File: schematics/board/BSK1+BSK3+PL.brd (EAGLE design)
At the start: 82 x 100 mm, 81 parts

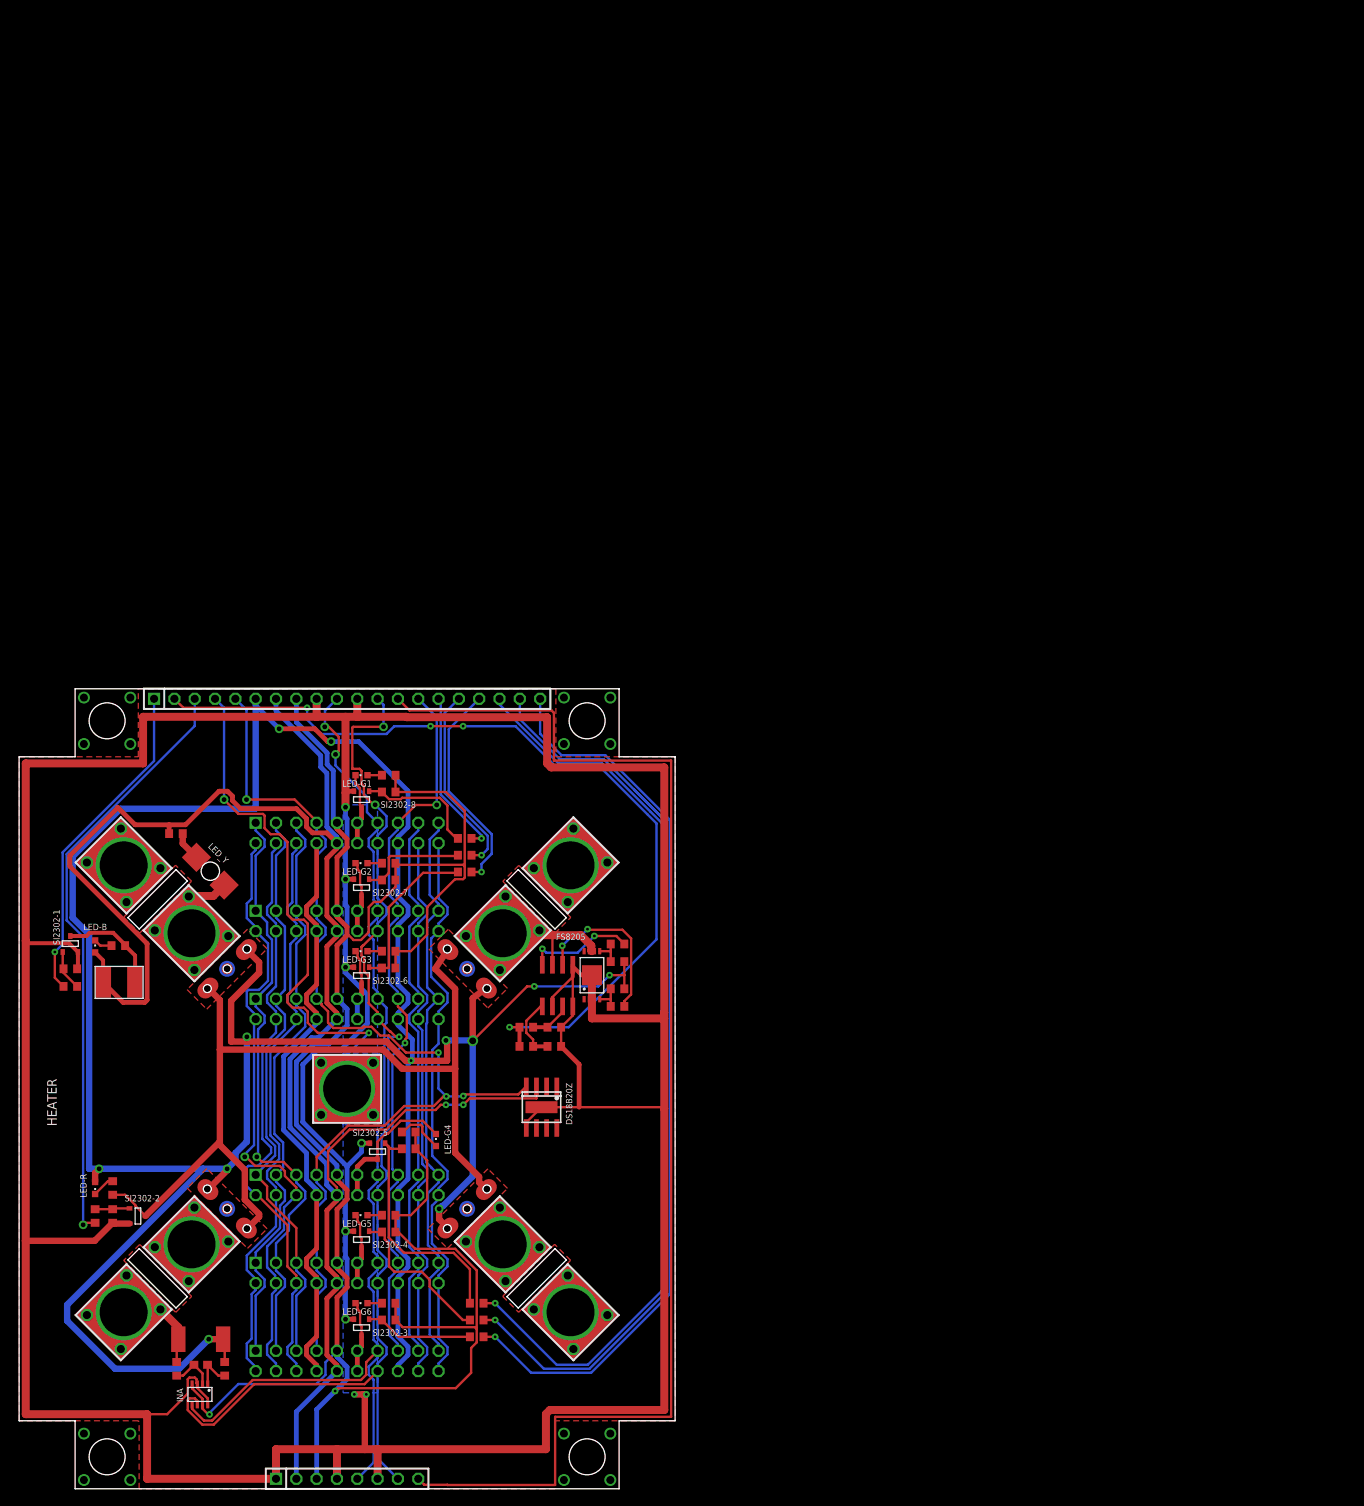
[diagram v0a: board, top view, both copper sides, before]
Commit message: Исправлены площадки механизмов Розе, соответствующие платы и герберы плат
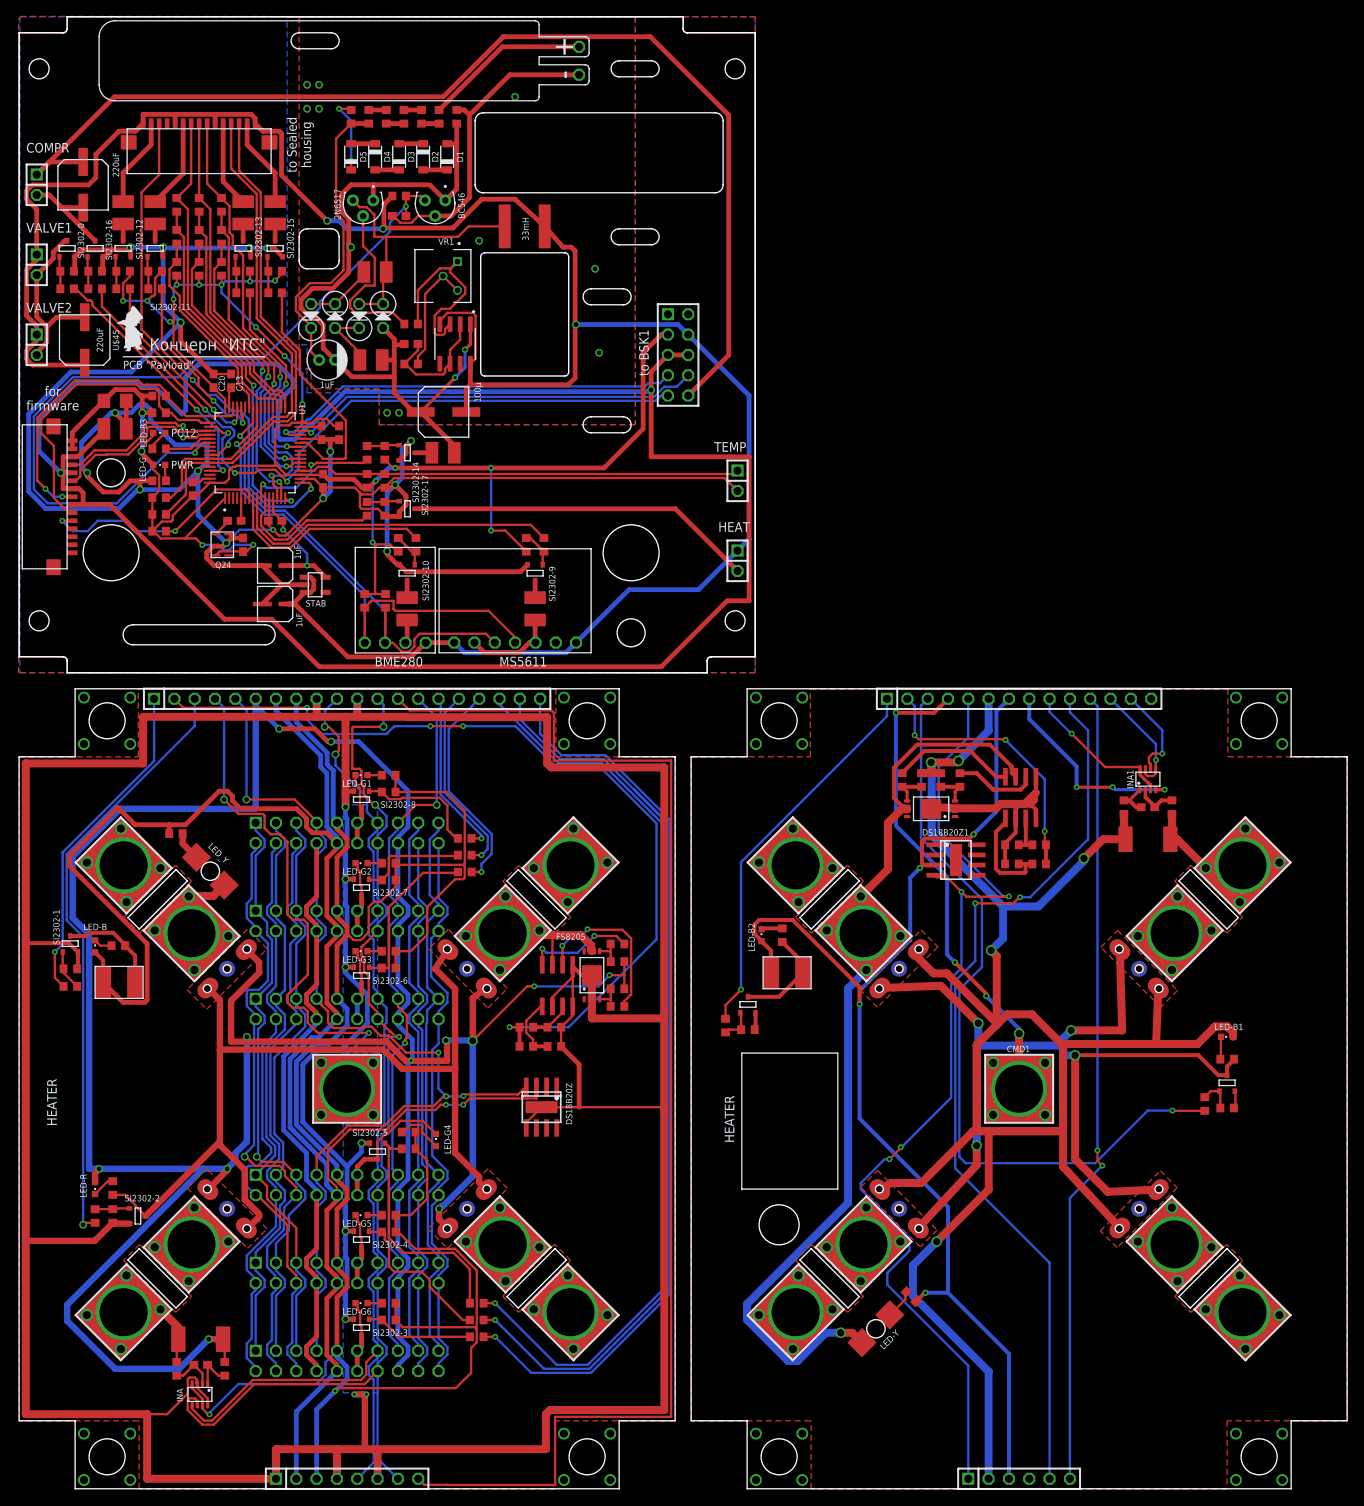
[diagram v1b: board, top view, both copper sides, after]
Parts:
- added 2N6517, BC546: DS1820, CanCubeSat:TO92/TO226
- added BKU1: (no value), pinheadCS:1X14
- added BME280: BME280BME280-PINS-ONLY, CanCubeSat:BME280-PINS-ONLY
- added BSK1: (no value), pinheadCS:1X06
- added BSK2: (no value), pinheadCS:2X05
- added C1: 0,1µ, rcl:C0603
- added C10: 10nF, rcl:C0603
- added C11: 100pF, rcl:C0603
- added C12, C14: 1uF, CanCubeSat:ECAP-SMD-D4
- added C13, C9: 2,2µ, rcl:C0603
- added C18, C2, C20, C3, C4, C6: 100nF, rcl:C0603
- added C19: 10µ, rcl:C1206
- added C5, C7: 22nF, rcl:C1210
- added C8: 1nF, rcl:C0603
- added CMD1: KCONNECTQUAD, CanCubeSat:KCONNECT_QUAD
- added COMPR, HEAT, TEMP, VALVE1, VALVE2: (no value), pinheadCS:1X02
- added D1, D2, D3, D4, D5: DIODE-MBR, CanCubeSat:SOD123
- added DS18B20Z1: DS18B20Z, CanCubeSat:SOIC8+HEAT_S
- added INA1: INA219AID, CanCubeSat:SOT23-8
- added LED-B1, LED-B2, LED-B3, LED-G: (no value), led:CHIPLED_0603
- added LED-Y: LAP4-BOTTOM, led:P47F-BOTTOM
- added MS5611: MS5611MS5611-PIN-ONLY, CanCubeSat:MS5611-PINS-ONLY
- added Q24: Q24, CanCubeSat:Q24
- added R100, R103, R105, R107, R40, R42, R58, R60, R63, R65, R68, R71, R82, R83, R84, R85, R86: 1M, resistor:R0603
- added R101, R104, R106, R108, R34, R35, R48, R49, R59, R61, R64, R66, R69, R72: 100R, resistor:R0603
- added R102, R57, R62, R67, R70, R73, R74: 0.05A, rcl:R1210
- added R109: 124k, resistor:R0603
- added R110, R81: 22k, resistor:R0603
- added R111, R112, R55, R56: 5k1, resistor:R0603
- added R36, R37, R87: 100k, resistor:R0603
- added R38, R39, R51, R54: 2k, resistor:R0603
- added R41: 1k5, resistor:R0603
- added R43: R01, rcl:R2512
- added R44, R45: 10R, resistor:R0603
- added R46, R47: 2k26, resistor:R0603
- added R50, R52, R53, R89, R90, R91, R92, R93, R96, R97, R98, R99: 10k, resistor:R0603
- added R78: 0.5A, rcl:R1210
- added R79: 1k, resistor:R0603
- added R80: 4k7, resistor:R0603
- added R88: 3k3, resistor:R0603
- added R94, R95: 200k, resistor:R0603
- added SI2302-0, SI2302-10, SI2302-11, SI2302-12, SI2302-13, SI2302-14, SI2302-15, SI2302-16, SI2302-17, SI2302-9, U$15, U$17: SI2302CDS, CanCubeSat:SOT23-3
- added STAB: ADP150AUJZ-3.3-R7, CanCubeSat:SOT23-5
- added U$10, U$11, U$12, U$5, U$6, U$7, U$8, U$9: KCONNECT, CanCubeSat:KCONNECT
- added U$13: FS8205A+, CanCubeSat:FS8205A+
- added U$14: MOCD, CanCubeSat:SOIC8
- added U$16: EM_HEAT, CanCubeSat:EM_HEAT
- added U$23, U$25, U$31, U$32: GRAFITGRAFIT4_2, CanCubeSat:GRAFIT4_2
- added U$33: PCB "BSK3", CanCubeSat:ITS-LOGO
- added U$34: 100µ, CanCubeSat:ECAP100-CMD
- added U$35, U$36, U$37, U$38: BA159, CanCubeSat:BA159
- added U$39: 1uF, CanCubeSat:ECAP1MK
- added U$40: DOSIM, CanCubeSat:DOSIM
- added U$41, U$43: FFC-CONNECT68611, CanCubeSat:68611
- added U$42: 33mH, CanCubeSat:RCH114NP
- added U$44, U$45: 220uF, CanCubeSat:ECAP220-CMD
- added U$46, U$47: PCB "Payload", CanCubeSat:ITS-LOGO
- added U1: STM32F405RGT6, STM32F405RGT6:QFP50P1200X1200X160-64N
- added U2: LMC555, LMC555CMX_NOPB:SOIC127P599X175-8N
- added VR1: 3362H-1-502LF, CanCubeSat:TRIM_3362H-1-502LF
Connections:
- new net 1: R39.2, U$15.3, U$16.2
- new net 1W1: BKU1.5, BSK1.1, DS18B20Z1.4
- new net 2: R41.2, U$17.3, U$23.P$1, U$23.P$4, U$25.P$1, U$25.P$4, U$31.P$1, U$31.P$4, U$32.P$1, U$32.P$4
- new net 3V1: BKU1.8, INA1.4
- new net 3V2: BSK2.3, C10.2, C18.2, C19.2, C2.2, C20.2, C6.2, LED-B3.A, LED-G.A, Q24.P$4, R100.2, R110.2, R111.1, R112.1, R50.2, R52.2, R53.2, R55.1, R56.1, R58.2, R60.2, R63.2, R65.2, R68.2, R71.2, R97.2, R98.2, R99.2, U$43.P$1, U$43.P$2, U1.1, U1.19, U1.32, U1.48, U1.64
- new net 4OXV: R66.1, U1.45
- new net 5V1: BKU1.7, BSK1.3, DS18B20Z1.3, LED-B2.A, R38.1, U$16.1
- new net 5V2: BME280.P$1, BSK2.4, C14.P+, HEAT.1, MS5611.P$1, MS5611.P$7, R88.1, STAB.P$1, STAB.P$3, U$34.P$2, U$41.P$1, U$41.P$10, U$41.P$15, U$41.P$5, U$42.P$1, U$45.P$1, U2.4, U2.8, VALVE1.1, VALVE2.1
- new net B3-CMD: BKU1.4, CMD1.1, CMD1.2, CMD1.3, CMD1.4, CMD1.P$1, CMD1.P$2
- new net B3-KHEAT: BKU1.1, R48.2
- new net B3-KVCC: BKU1.2, R46.2, R47.2
- new net B3-ROZE: BKU1.3, R49.2
- new net B5-KHEAT: BKU1.10, BSK1.5
- new net BME280-EXT: R61.1, U1.8
- new net BME280-INT: R101.1, U1.27
- new net BUS+1: BKU1.6, BSK1.2, LED-B1.A, R36.1, R37.2, R43.2, R44.1, U$23.P$2, U$23.P$5, U$25.P$2, U$25.P$5, U$31.P$2, U$31.P$5, U$32.P$2, U$32.P$5
- new net BUS+2: BSK2.10, COMPR.1, U$44.P$1
- new net CO: R91.1, U$41.P$7, U1.16
- new net COMPR: R106.1, U1.57
- new net CTRL-CO-1: R91.2, R96.1, U1.35
- new net CTRL-CO-2: R96.2, R97.1, U1.42
- new net CTRL-NH3-1: R90.2, R93.1, U1.33
- new net CTRL-NH3-2: R93.2, R98.1, U1.34
- new net CTRL-NO2-1: R89.2, R92.1, U1.23
- new net CTRL-NO2-2: R92.2, R99.1, U1.22
- new net DOS-G: 2N6517.1, BC546.1, C4.1, C7.2, D1.A, R73.1, R87.2, U$34.P$1, U$35.P$1, U$39.P$2, U2.1
- new net DOSE: BC546.3, C11.2, R88.2, U1.54
- new net DOSIM: R72.1, U1.10
- new net G-4OXV: R67.1, U$41.P$2
- new net G-BME: R102.1, U$41.P$14
- new net G-MICS: R74.1, U$41.P$6
- new net G-MS: R70.1, U$41.P$11
- new net GND-4OXV: R67.2, SI2302-12.3
- new net GND-BME-EXT: R62.2, SI2302-10.3
- new net GND-BME-INT: R102.2, SI2302-15.3
- new net GND-COMPR: COMPR.2, SI2302-16.3, U$44.P$2
- new net GND-DOSIM: R73.2, SI2302-14.3
- new net GND-HEAT: HEAT.2, SI2302-17.3
- new net GND-MICS: R74.2, SI2302-11.3
- new net GND-MS-EXT: R57.2, SI2302-9.3
- new net GND-MS-INT: R70.2, SI2302-13.3
- new net GND-OUT: BSK2.5, BSK2.6, R78.2, U$43.P$3, U$43.P$5, U$43.P$7, U$43.P$9
- new net GND-VALVE: SI2302-0.3, U$45.P$2, VALVE1.2, VALVE2.2
- new net GND4: BKU1.14, BKU1.9, BSK1.4, DS18B20Z1.5, DS18B20Z1.HEAT, INA1.3, INA1.8, R40.2, R42.2, R94.1, R95.1, U$13.23, U$13.HEAT, U$14.2, U$14.4, U$14.5, U$15.2, U$17.2
- new net GND9: C10.1, C12.P-, C13.1, C14.P-, C18.1, C19.1, C2.1, C20.1, C3.2, C6.1, C9.1, Q24.P$2, R103.2, R105.2, R107.2, R109.1, R54.1, R78.1, SI2302-0.2, SI2302-10.2, SI2302-11.2, SI2302-12.2, SI2302-13.2, SI2302-14.2, SI2302-15.2, SI2302-16.2, SI2302-17.2, SI2302-9.2, STAB.P$2, TEMP.2, U1.12, U1.18, U1.28, U1.60, U1.63
- new net HEAT: R108.1, U1.11
- new net MICS: R64.1, U1.44
- new net MS5611-EXT: R59.1, U1.9
- new net MS5611-INT: R69.1, U1.26
- new net N$100: R105.1, R106.2, SI2302-16.1
- new net N$101: R107.1, R108.2, SI2302-17.1
- new net N$102: C12.P+, C3.1, STAB.P$5, U1.13
- new net N$103: LED-G.C, R54.2
- new net N$33: R35.1, R36.2, U$13.5
- new net N$39: R34.1, R37.1, U$13.4
- new net N$40: LED-Y.A, R38.2
- new net N$41: LED-B2.C, R39.1
- new net N$42: LED-B1.C, R41.1
- new net N$43: C1.1, INA1.1, R44.2
- new net N$44: C1.2, INA1.2, R45.2
- new net N$45: R46.1, R94.2, U$14.1
- new net N$46: R47.1, R95.2, U$14.3
- new net N$63: R40.1, R48.1, U$15.1
- new net N$64: R42.1, R49.1, U$17.1
- new net N$65: R51.1, U1.53
- new net N$66: C13.2, U1.47
- new net N$67: C9.2, U1.31
- new net N$68: C8.1, U1.5
- new net N$69: LED-B3.C, R51.2
- new net N$70: C8.2, Q24.P$3
- new net N$71: R58.1, R59.2, SI2302-9.1
- new net N$72: MS5611.P$3, MS5611.P$6, R57.1
- new net N$73: R60.1, R61.2, SI2302-10.1
- new net N$74: BME280.P$2, R62.1
- new net N$75: R63.1, R64.2, SI2302-11.1
- new net N$76: R65.1, R66.2, SI2302-12.1
- new net N$77: R68.1, R69.2, SI2302-13.1
- new net N$78: R71.1, R72.2, SI2302-14.1
- new net N$79: C4.2, R79.1, U2.2, U2.6
- new net N$80: R79.2, VR1.2, VR1.3
- new net N$81: R80.2, U2.3, VR1.1
- new net N$82: 2N6517.2, R80.1
- new net N$83: 2N6517.3, C5.1, U$35.P$2, U$36.P$1, U$42.P$2
- new net N$84: C7.1, U$36.P$2, U$37.P$1
- new net N$85: C5.2, U$37.P$2, U$38.P$1
- new net N$86: R81.2, R82.2, U$38.P$2, U$39.P$1
- new net N$87: D1.C, D2.A
- new net N$88: D2.C, D3.A
- new net N$89: D3.C, D4.A
- new net N$90: D4.C, D5.A
- new net N$91: D5.C, R81.1
- new net N$92: R82.1, R83.1
- new net N$93: R83.2, R84.2
- new net N$94: R84.1, R85.1
- new net N$95: R85.2, R86.2
- new net N$96: R86.1, U$40.P$1
- new net N$97: BC546.2, C11.1, R87.1, U$40.P$2
- new net N$98: R100.1, R101.2, SI2302-15.1
- new net N$99: R103.1, R104.2, SI2302-0.1
- new net NH3: R90.1, U$41.P$8, U1.15
- new net NO2: R89.1, U$41.P$9, U1.14
- new net NRST: R50.1, U$43.P$11, U1.7
- new net O2: U$41.P$3, U1.17
- new net OC1: R34.2, U$14.6
- new net OD1: R35.2, U$14.8
- new net RX-S: U$43.P$4, U1.52
- new net SCL-TM1: BKU1.12, INA1.5, INA1.7
- new net SCL-TM2: BSK2.7, U1.29
- new net SDA-TM1: BKU1.13, INA1.6
- new net SDA-TM2: BSK2.8, U1.30
- new net SENS-EXT-SCL: BME280.P$3, MS5611.P$5, R112.2, U1.41
- new net SENS-EXT-SDA: BME280.P$4, MS5611.P$4, R111.2, U1.40
- new net SENS-INT-SCL: R55.2, U$41.P$12, U1.58
- new net SENS-INT-SDA: R56.2, U$41.P$13, U1.59
- new net SINS-KVCC: BKU1.11, BSK1.6
- new net SP+4: U$5.1, U$5.2, U$5.3, U$5.4, U$5.P$1, U$5.P$2
- new net SP+5: U$6.1, U$6.2, U$6.3, U$6.4, U$6.P$1, U$6.P$2
- new net SP+6: U$9.1, U$9.2, U$9.3, U$9.4, U$9.P$1, U$9.P$2
- new net SP+7: R43.1, R45.1, U$11.1, U$11.2, U$11.3, U$11.4, U$11.P$1, U$11.P$2
- new net SP-4: U$12.1, U$12.2, U$12.3, U$12.4, U$12.P$1, U$12.P$2
- new net SP-5: U$7.1, U$7.2, U$7.3, U$7.4, U$7.P$1, U$7.P$2
- new net SP-6: U$10.1, U$10.2, U$10.3, U$10.4, U$10.P$1, U$10.P$2
- new net SP-7: LED-Y.C, U$13.67, U$14.7, U$8.1, U$8.2, U$8.3, U$8.4, U$8.P$1, U$8.P$2
- new net SWC: R53.1, U$43.P$10, U1.49
- new net SWD: R52.1, U$43.P$8, U1.46
- new net TEMP: R109.2, R110.1, TEMP.1, U1.20
- new net TIME1: BSK2.9, U1.50
- new net TX-S: U$43.P$6, U1.51
- new net VALVE: R104.1, U1.61
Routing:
- net GND9: track 0.00 -> 340.6 mm, vias 0 -> 16
- net 5V2: track 0.00 -> 290.7 mm, vias 0 -> 3
- net 3V2: track 0.00 -> 270.7 mm, vias 0 -> 21
- net GND-OUT: track 0.00 -> 265.5 mm, vias 0 -> 2
- net BUS+1: track 0.00 -> 248.4 mm, vias 0 -> 5
- net 5V1: track 0.00 -> 148.3 mm, vias 0 -> 4
- net 2: track 0.00 -> 142.9 mm, vias 0 -> 4
- net BUS+2: track 0.00 -> 141.3 mm
- net 1W1: track 0.00 -> 127.5 mm, vias 0 -> 4
- net SP-7: track 0.00 -> 125.8 mm, vias 0 -> 1
- net B5-KHEAT: track 0.00 -> 113.8 mm, vias 0 -> 2
- net SINS-KVCC: track 0.00 -> 99.8 mm, vias 0 -> 2
- net DOS-G: track 0.00 -> 99.6 mm, vias 0 -> 13
- net DOSE: track 0.00 -> 98.7 mm, vias 0 -> 2
- net B3-ROZE: track 0.00 -> 95.6 mm, vias 0 -> 1
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- added copper zone on layer 1, net DOS-G
- added copper zone on layer 16, net DOS-G
- added copper zone on layer 1, net GND4
- added copper zone on layer 1, net GND5
- added copper zone on layer 1, net GND6
- added copper zone on layer 1, net GND7
- added copper zone on layer 1, net GND8
- added copper zone on layer 1, net GND9
- added copper zone on layer 16, net GND9
- added copper zone on layer 1, net HEAT4
- added copper zone on layer 1, net HEAT5
- added copper zone on layer 1, net HEAT6
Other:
- board size 82 x 100 mm -> 166 x 184 mm
- board text added: "PC12"
- board text added: "PWR"
- board text added: "for firmware"
- board text added: "to BSK1"
- board text added: "to Sealed housing"
